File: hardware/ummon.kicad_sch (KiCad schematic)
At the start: 0 parts

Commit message: :sparkles: Initialize kicad project
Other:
- title: UmMon V0.1 -> (none)
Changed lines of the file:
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@@
 	(generator_version "10.0")
 	(paper "A4")
-	(title_block
-		(title "UmMon V0.1")
-	)
 	(sheet_instances
 		(path "/"

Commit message: :sparkles: Add reccomended sensor setups
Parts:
- added C1, C5, C6, C7: 100nF, symbol Device:C_Small
- added C2, C3: 1µF, symbol Device:C_Small
- added C4: 10µF, symbol Device:C_Small
- added R1: 4.7Ω, symbol Device:R_Small
- added U1: ESP32-C6-WROOM-1-N8, parts:WIRELM-SMD_ESP32-C6-WROOM-1, symbol parts:ESP32-C6-WROOM-1-N8
- added U2: SCD41-D-R2, parts:LGA-20_L10.1-W10.1-P1.25-TL, symbol parts:SCD41-D-R2
- added U3: SGP41-D-R4, parts:DFN-6_L2.4-W2.4-P0.80-TL-EP, symbol parts:SGP41-D-R4
- added U4: SHT41-AD1B-R2, parts:DFN-4_L1.5-W1.5-SHT41-AD1B-R2, symbol parts:SHT41-AD1B-R2
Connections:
- new net: C2.1, C7.1, R1.2, U3.1 (VDD)
- new net +3.3V: C1.1, C3.1, C4.1, C5.1, C6.1, R1.1, U2.19 (VDDH), U2.7 (VDD), U3.5 (VDDH), U4.3 (VDD)
- new net GND: C1.2, C2.2, C3.2, C4.2, C5.2, C6.2, C7.2, U2.20 (GND), U2.21 (GND), U2.6 (GND), U3.2 (VSS), U3.4 (n/a), U3.7 (EP), U4.4 (VSS)
- new net I2C_SCL: U2.9 (SCL), U3.6 (SCL), U4.2 (SCL)
- new net I2C_SDA: U2.10 (SDA), U3.3 (SDA), U4.1 (SDA)
- no-connect marks 0 -> 14
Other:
- title: (none) -> Ummon

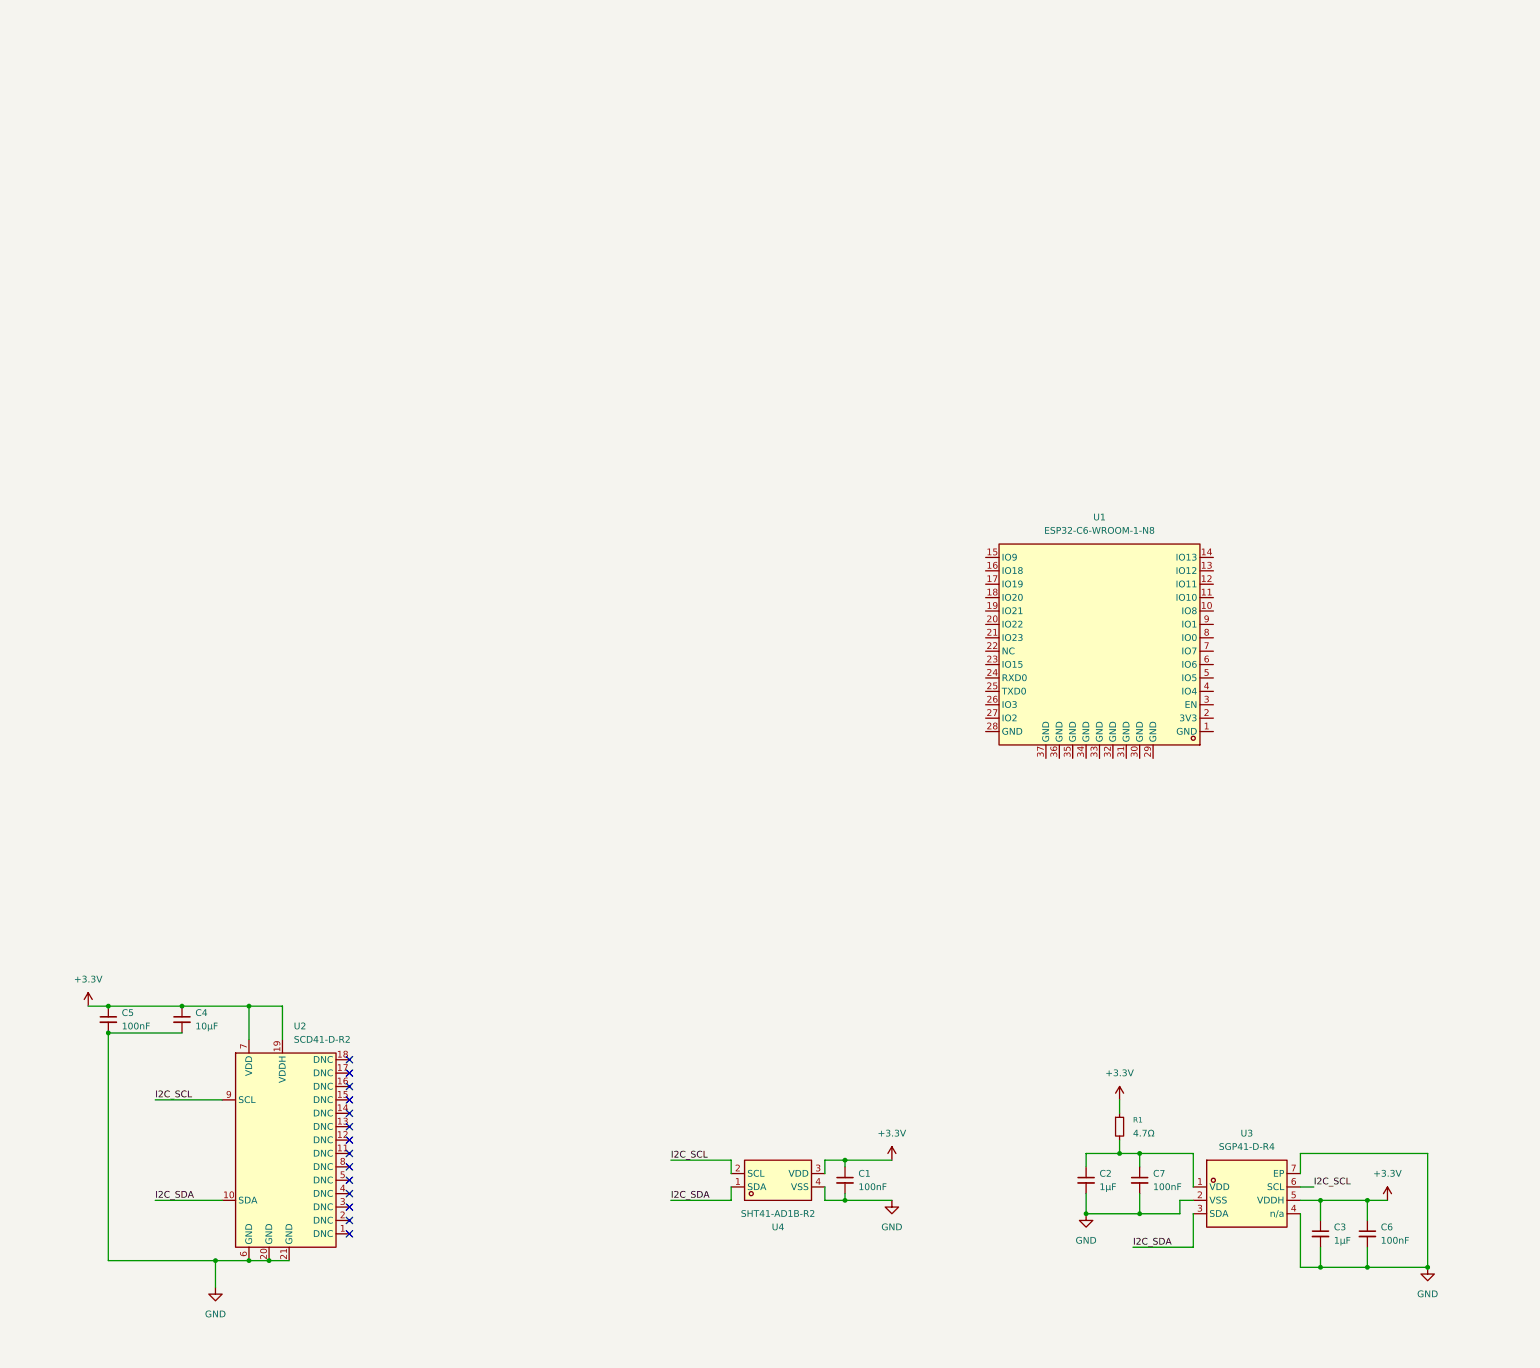
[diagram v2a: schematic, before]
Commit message: :sparkles: Add microcontroller with boot/reset pins
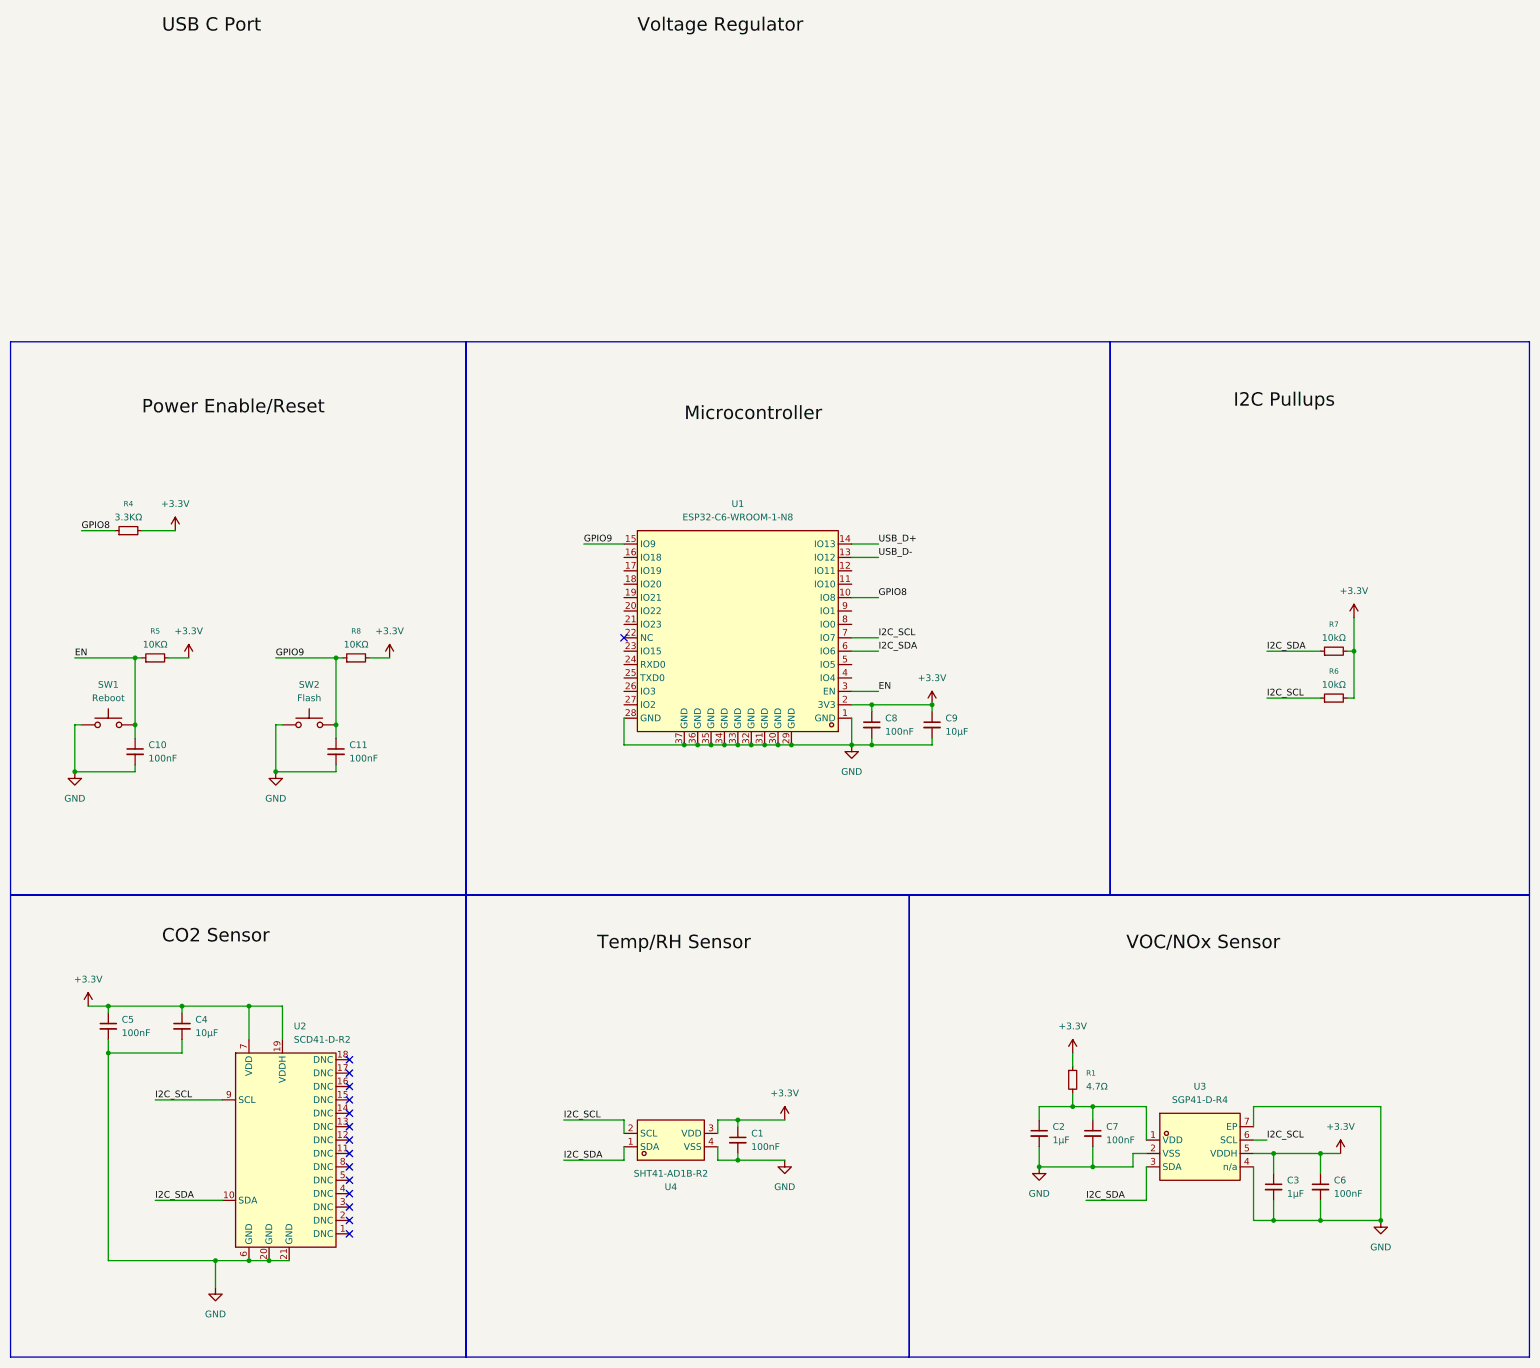
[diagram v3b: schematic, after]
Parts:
- added C10, C11, C8: 100nF, symbol Device:C_Small
- added C9: 10µF, symbol Device:C_Small
- added R4: 3.3KΩ, symbol Device:R_Small
- added R5, R8: 10KΩ, symbol Device:R_Small
- added R6, R7: 10kΩ, symbol Device:R_Small
- added SW1: Reboot, symbol Switch:SW_Push
- added SW2: Flash, symbol Switch:SW_Push
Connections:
- net +3.3V: now also U1.2 (3V3), C8.1, C9.1, R4.2, R5.2, R6.2, R7.2, R8.2
- net GND: now also U1.1 (GND), U1.28 (GND), U1.29 (GND), U1.30 (GND), U1.31 (GND), U1.32 (GND), U1.33 (GND), U1.34 (GND), U1.35 (GND), U1.36 (GND), U1.37 (GND), C10.2, C11.2, C8.2, C9.2, SW1.1, SW2.1
- net I2C_SCL: now also U1.7 (IO7), R6.1
- net I2C_SDA: now also U1.6 (IO6), R7.1
- net GPIO8: now reaches U1.10 (IO8)
- net GPIO8: now also R4.1
- net USB_D-: now reaches U1.13 (IO12)
- net USB_D+: now reaches U1.14 (IO13)
- net GPIO9: now reaches U1.15 (IO9)
- net GPIO9: now also C11.1, R8.1, SW2.2
- net EN: now reaches U1.3 (EN)
- net EN: now also C10.1, R5.1, SW1.2
- no-connect marks 14 -> 15
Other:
- moved on the sheet: C1, C2, C3, C4, C5, C6, C7, R1, U1, U3, U4

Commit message: :sparkles: Add header for spi, i2c and uart
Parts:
- added C12, C13: 100nF, symbol Device:C_Small
- added J1: Conn_01x08_Pin, symbol Connector:Conn_01x08_Pin
- added J2: Conn_01x05_Pin, symbol Connector:Conn_01x05_Pin
- added J3, J4: Conn_01x04_Pin, symbol Connector:Conn_01x04_Pin
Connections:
- net +3.3V: now also C13.1, J1.1 (Pin_1), J4.1 (Pin_1)
- net GND: now also C12.2, C13.2, J1.2 (Pin_2), J2.4 (Pin_4), J3.4 (Pin_4), J4.4 (Pin_4)
- net I2C_SCL: now also J3.3 (Pin_3), J4.3 (Pin_3)
- net I2C_SDA: now also J3.2 (Pin_2), J4.2 (Pin_2)
- net EPD_DIN: now reaches U1.16 (IO18)
- net EPD_DIN: now also J1.3 (Pin_3)
- net EPD_SCK: now reaches U1.17 (IO19)
- net EPD_SCK: now also J1.4 (Pin_4)
- net EPD_CS: now reaches U1.18 (IO20)
- net EPD_CS: now also J1.5 (Pin_5)
- net EPD_DC: now reaches U1.19 (IO21)
- net EPD_DC: now also J1.6 (Pin_6)
- net EPD_RST: now reaches U1.20 (IO22)
- net EPD_RST: now also J1.7 (Pin_7)
- net EPD_BUSY: now reaches U1.21 (IO23)
- net EPD_BUSY: now also J1.8 (Pin_8)
- net RX: now reaches U1.24 (RXD0)
- net RX: now also J2.2 (Pin_2)
- net TX: now reaches U1.25 (TXD0)
- net TX: now also J2.3 (Pin_3)
- new net +5V: C12.1, J2.5 (Pin_5), J3.1 (Pin_1)
- new net H_PRESENCE: J2.1 (Pin_1)
